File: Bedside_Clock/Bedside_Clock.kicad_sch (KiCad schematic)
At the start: 42 parts, among them J1 USBC_USB2.0, SW1 COLOR, SW2 MODE, SW3 BOOT, SW4 RESET, U1 ESP32-C3-MINI-1, U2 USBLC6-2SC6, U3 VCNL4040M3OE, U4 SN74LVC2T45DCUR

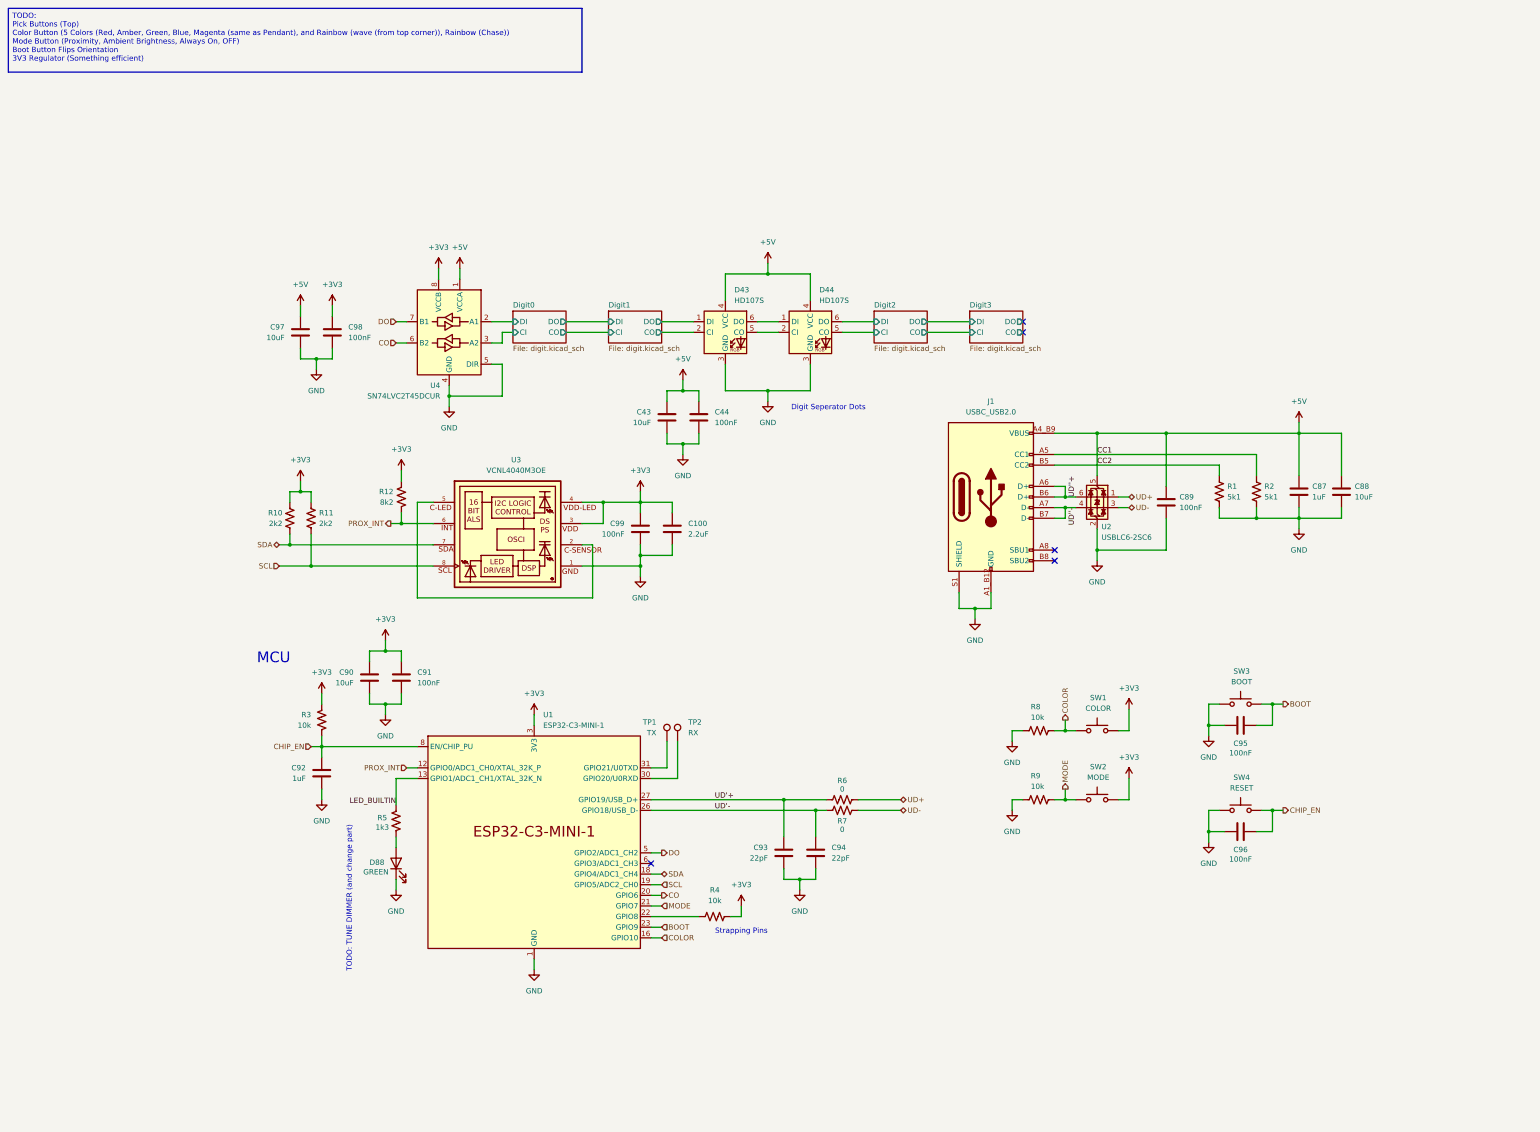
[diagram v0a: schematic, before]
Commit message: [HW] Find all parts and finish layout
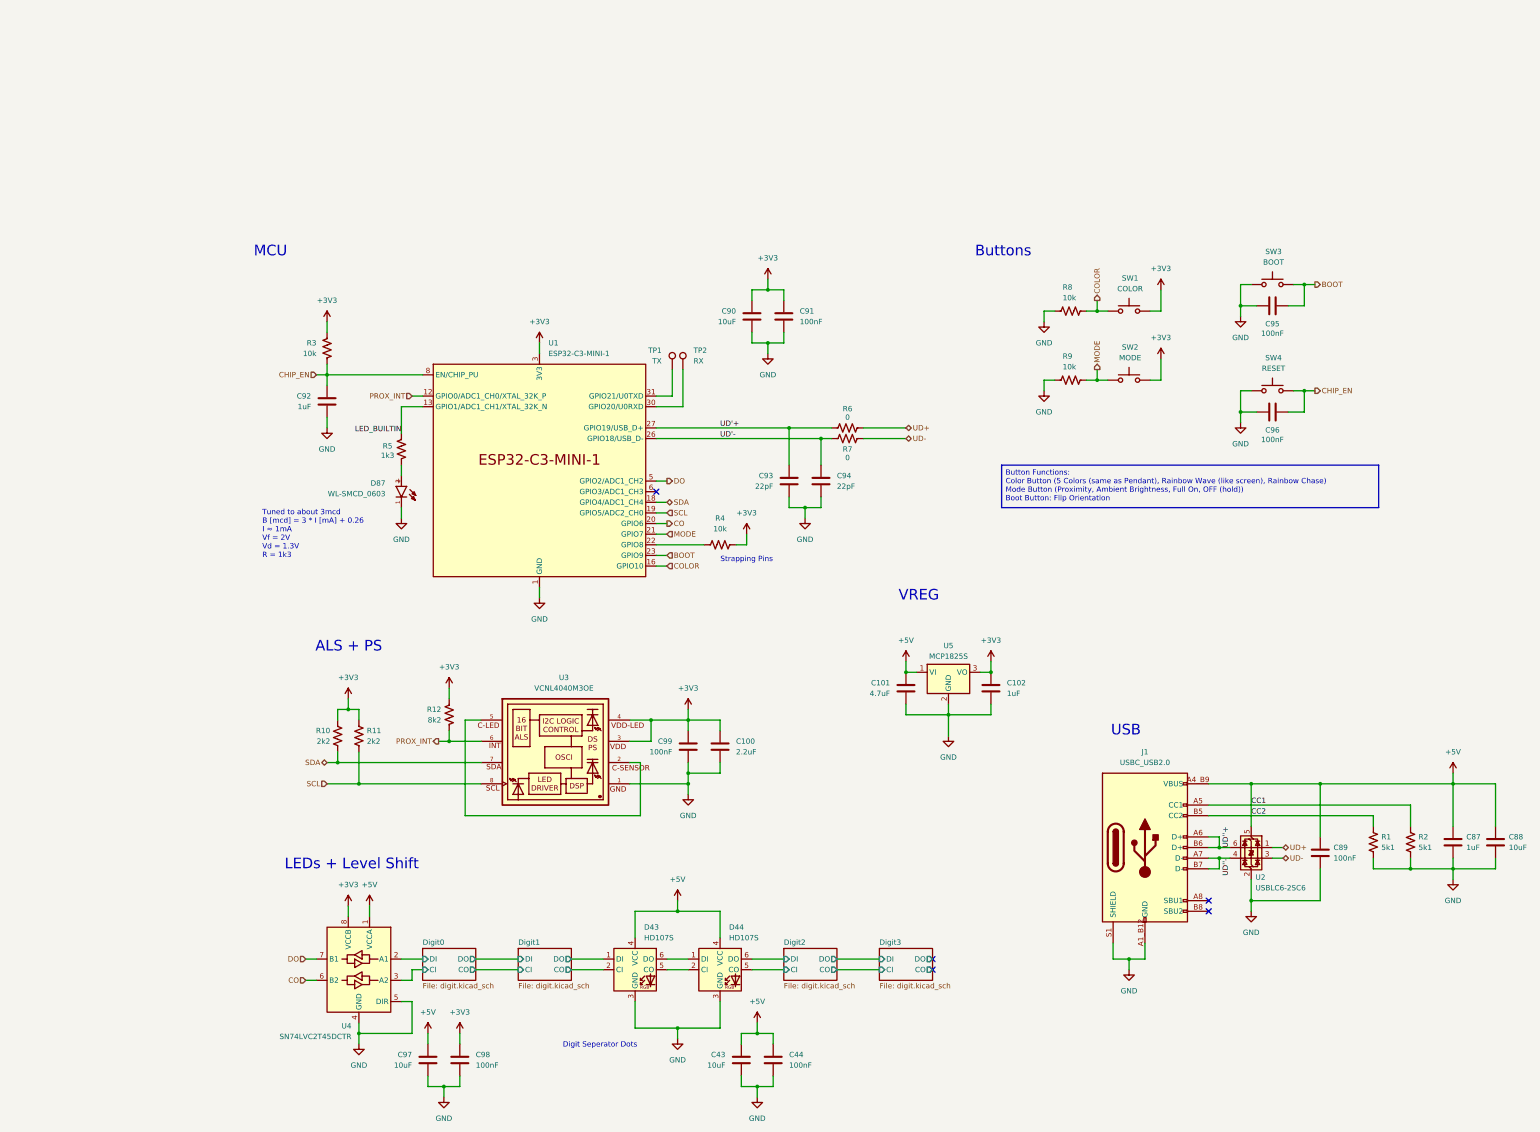
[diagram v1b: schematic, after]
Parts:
- removed D88: GREEN, symbol Device:LED
- added C101: 4.7uF, Capacitor_SMD:C_0603_1608Metric, symbol Device:C
- added C102: 1uF, Capacitor_SMD:C_0603_1608Metric, symbol Device:C
- added D87: WL-SMCD_0603, 150060VS55040:WL-SMCD_0603, symbol WL-SMCD_0603:WL-SMCD_0603
- added U5: MCP1825S, Package_TO_SOT_SMD:SOT-223-3_TabPin2, symbol Regulator_Linear:MCP1825S
- SW1, SW2, SW3, SW4: footprint (none) -> TL6330AF200Q:SW_TL6330AF200Q
- U4: value SN74LVC2T45DCUR -> SN74LVC2T45DCTR; footprint Package_SO:VSSOP-8_2.3x2mm_P0.5mm -> SN74LVC2T45DCTR:SOP65P400X130-8N
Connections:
- net +3V3: now also SW1.2, SW2.2, C102.1, U5.3 (VO)
- net +5V: now also C101.1, U5.1 (VI)
- net BOOT: now also SW3.2
- net CHIP_EN: now also SW4.2
- net COLOR: now also SW1.3, SW1.4; no longer SW1.2
- net GND: now also SW3.3, SW3.4, SW4.3, SW4.4, C101.2, C102.2, D87.1, U5.2 (GND); no longer SW3.2, SW4.2
- net MODE: now also SW2.3, SW2.4; no longer SW2.2
- net at R5.1: now also D87.2
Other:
- note added: "ALS + PS"
- note added: "Buttons"
- note added: "LEDs + Level Shift"
- note added: "Tuned to about 3mcd B [mcd] = 3 * I [mA] + 0.26 I ≈ 1mA Vf = 2V Vd = 1.3V R = 1k3"
- note added: "USB"
- note added: "VREG"
- note removed: "TODO: TUNE DIMMER (and change part)"
- moved on the sheet: C100, C43, C44, C87, C88, C89, C90, C91, C92, C93, C94, C95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

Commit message: [Docs] Add Schematics and Renders Add Diodes, Switches, and Conns to BOM Need Resistors and Capacitors now
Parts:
- C43: value 10uF -> 100nF
- R5: value 1k3 -> 1k43
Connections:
- net +5V: no longer J1.A5 (CC1), J1.B5 (CC2), R1.2, R2.2
- new net CC1: J1.A5 (CC1), R2.2
- new net CC2: J1.B5 (CC2), R1.2
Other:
- note added: "Ambient Light and Proximity Sensor"
- note added: "Strapping Pins: - Chip EN - Reset - GPIO2 - Ignore - GPIO8 - Pull Up - GPIO9 - Internal Pull Up"
- note added: "Tuned to about 2.5mcd B [mcd] = 3 * I [mA] + 0.26 I ≈ 0.9mA Vf = 2V Vd = 1.3V R = 1k43"
- note removed: "ALS + PS"
- note removed: "Strapping Pins"
- note removed: "Tuned to about 3mcd B [mcd] = 3 * I [mA] + 0.26 I ≈ 1mA Vf = 2V Vd = 1.3V R = 1k3"
- moved on the sheet: C100, C101, C102, C43, C44, C87, C88, C89, C90, C91, C92, C93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

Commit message: [Docs] Finish BOM
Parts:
- R10, R11: value 2k2 -> 3k3
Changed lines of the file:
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@@
 			)
 		)
-		(property "Value" "2k2"
+		(property "Value" "3k3"
 			(at 53.975 116.84 0)
 			(effects
@@
 			)
 		)
-		(property "Value" "2k2"
+		(property "Value" "3k3"
 			(at 45.212 116.84 0)
 			(effects

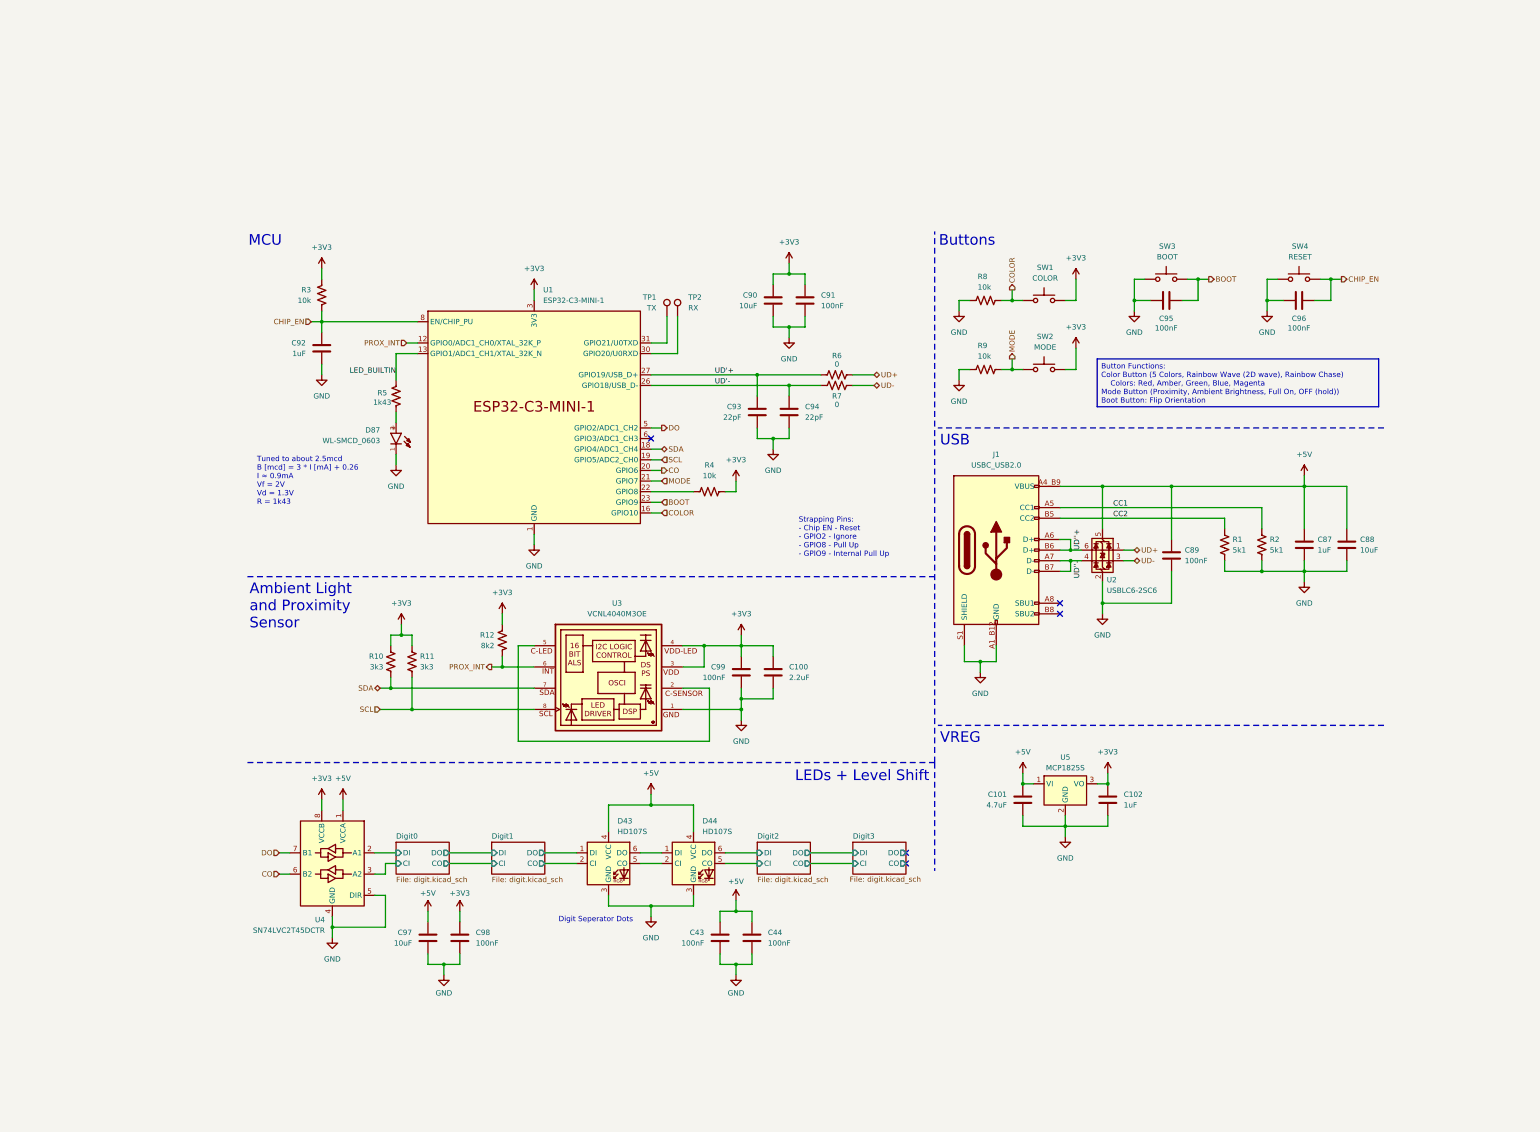
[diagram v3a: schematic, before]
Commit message: [HW] Add Series Resistors for SPI/LED Data (can be replaced with 0Ω if necessary) SPI Routing clean up to allow series resistors Also cleaned up some usage notes
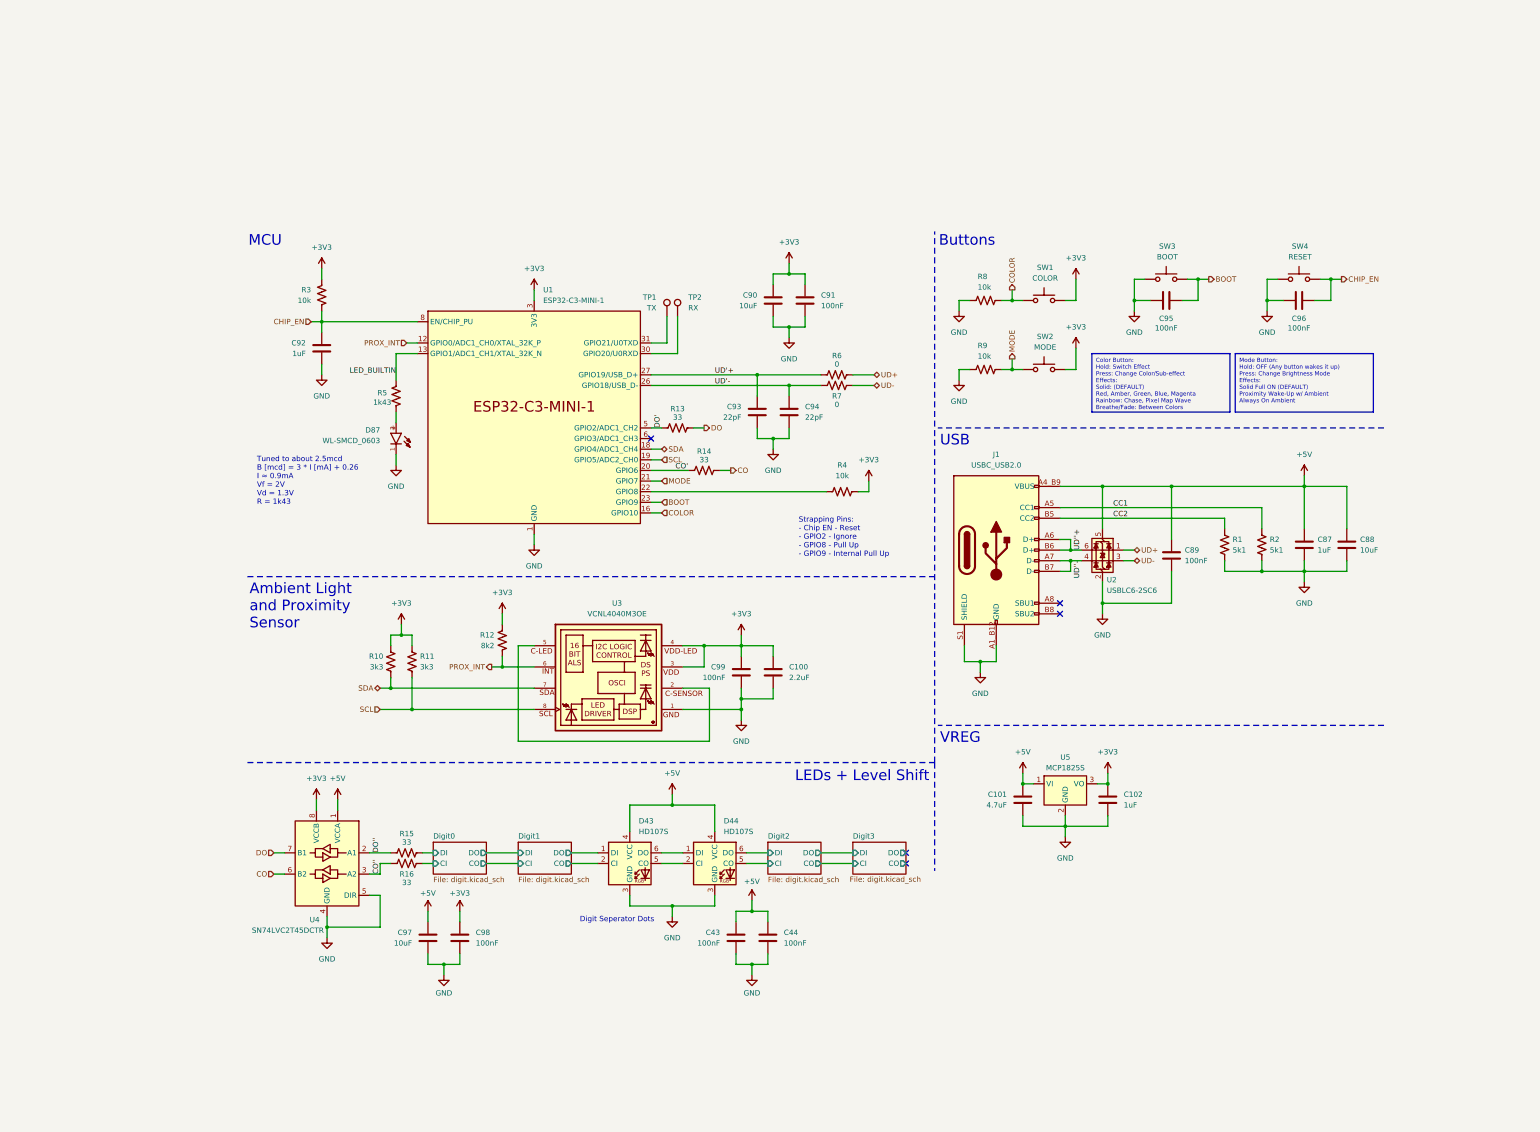
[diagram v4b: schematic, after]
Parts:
- added R13, R14, R15, R16: 33, Resistor_SMD:R_0603_1608Metric, symbol Device:R_US
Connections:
- net CO: now also R14.2; no longer U1.20 (GPIO6)
- net DO: now also R13.2; no longer U1.5 (GPIO2/ADC1_CH2)
- net Digit0/CI: now also R16.2; no longer U4.3 (A2)
- net Digit0/DI: now also R15.2; no longer U4.2 (A1)
- new net CO': R14.1, U1.20 (GPIO6)
- new net CO'': R16.1, U4.3 (A2)
- new net DO': R13.1, U1.5 (GPIO2/ADC1_CH2)
- new net DO'': R15.1, U4.2 (A1)
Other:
- moved on the sheet: C43, C44, D43, D44, R4, U4
